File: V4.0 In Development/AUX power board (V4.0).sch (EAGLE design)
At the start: 90 parts, among them U1 ATMEGA328P_TQFP, U2 TPS5405DR, U3 LTC4365HTS8TRMPBFTSOT-23_TS8-M

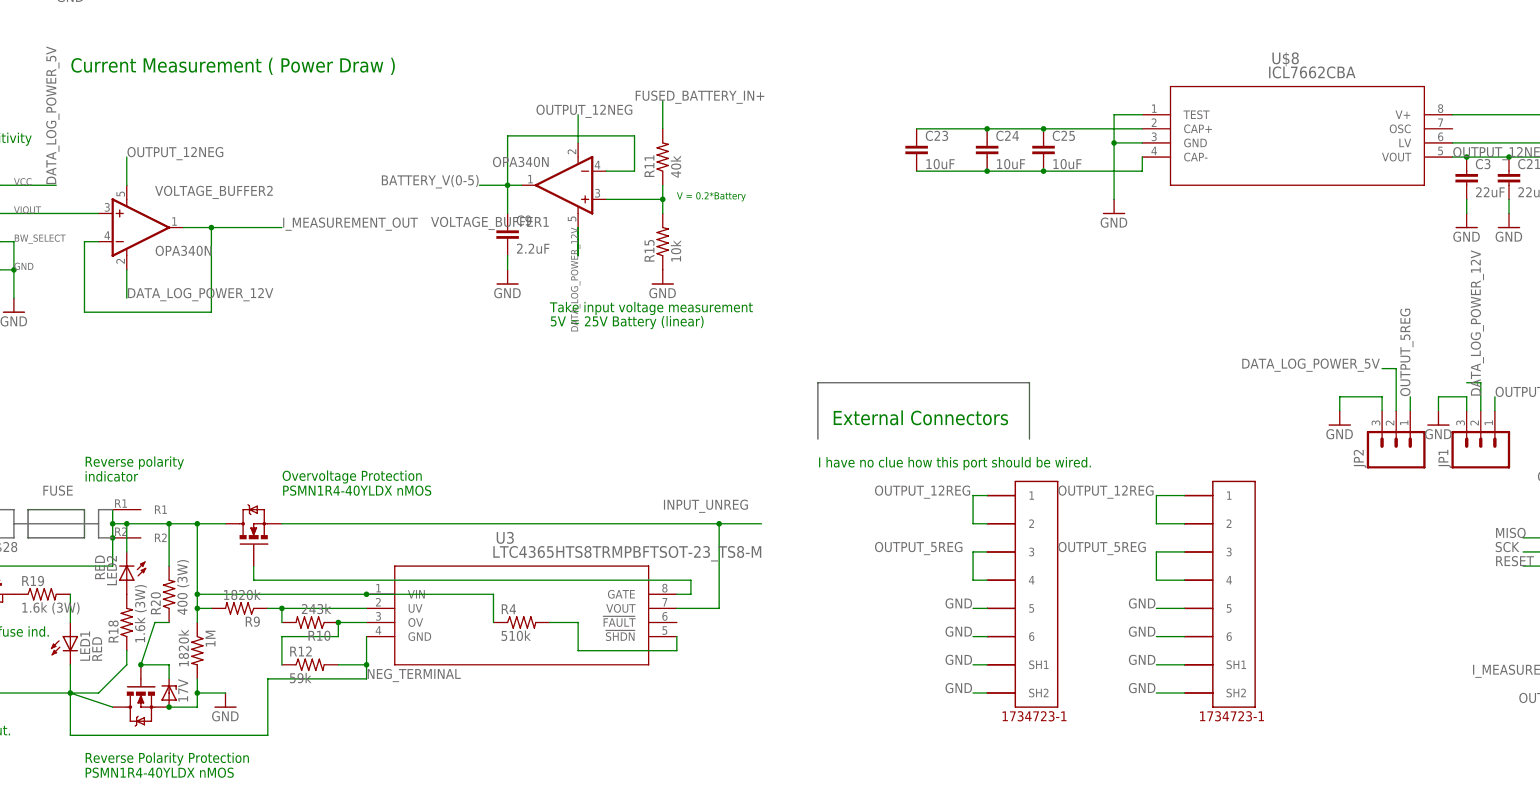
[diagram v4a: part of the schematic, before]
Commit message: Changed to a SOIC opamp
Easier to solder. Had issues with the smaller opamps in the previous
version.

The op-amp i spec'ed out also has a small DC bias (1mV and uses 45uA to
bias)
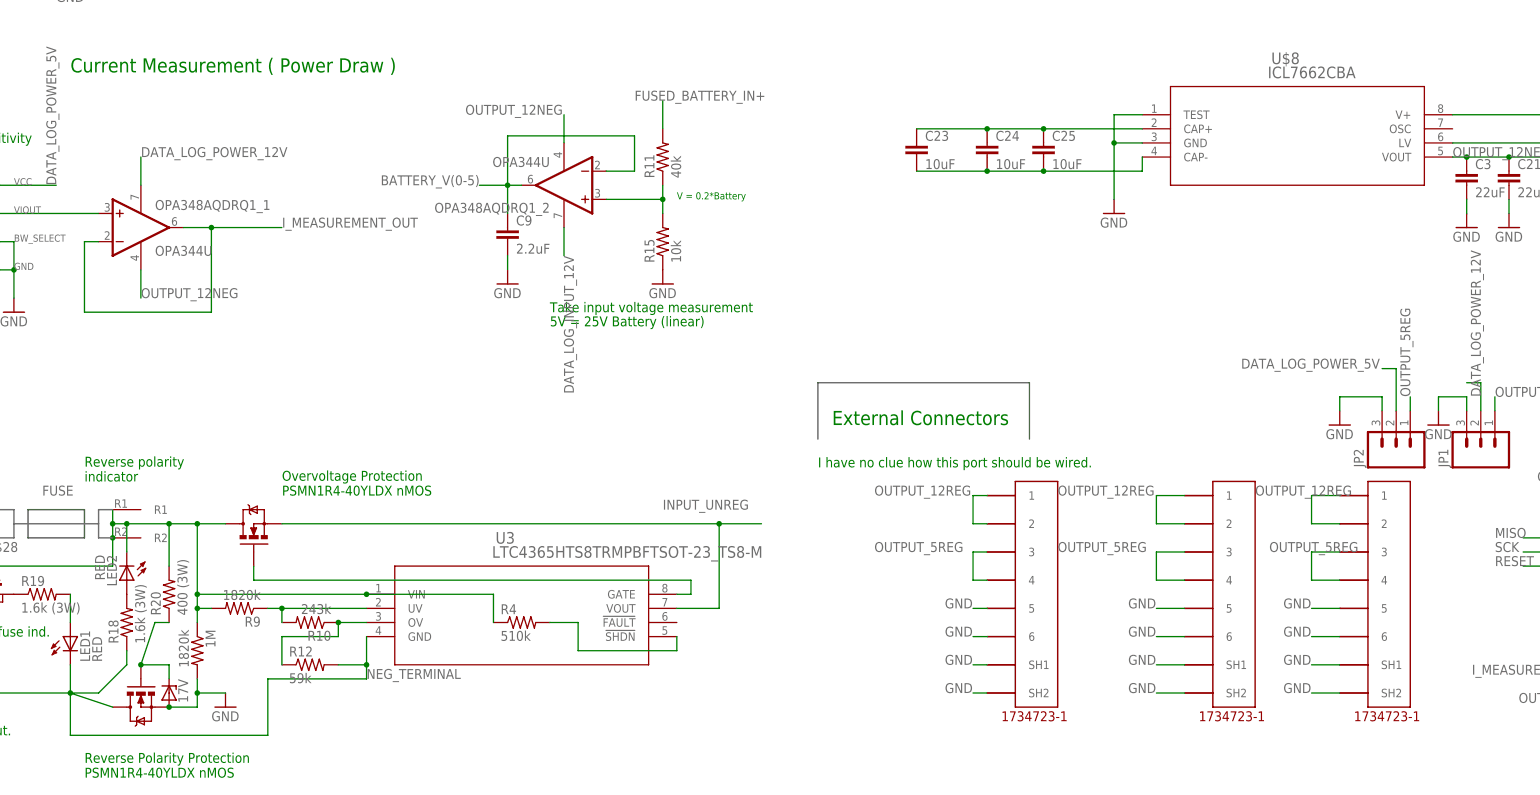
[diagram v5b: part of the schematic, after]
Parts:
- removed VOLTAGE_BUFFER1, VOLTAGE_BUFFER2: OPA340N, burr-brown:OPA340N
- added OPA348AQDRQ1_1, OPA348AQDRQ1_2: OPA344U, linear:OPA344U
- added U$10: 5555140-6, 5555140-6 RJ11:5555140-6
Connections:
- new net DATA_LOG_INPUT_12V: OPA348AQDRQ1_2.V+
- net BATTERY_V(0-5): now also OPA348AQDRQ1_2.-IN, OPA348AQDRQ1_2.OUT; no longer VOLTAGE_BUFFER1.-IN, VOLTAGE_BUFFER1.OUT
- net DATA_LOG_POWER_12V: now also OPA348AQDRQ1_1.V+; no longer VOLTAGE_BUFFER1.V+
- net GND: now also U$10.5, U$10.6, U$10.SH1, U$10.SH2
- net I_MEASUREMENT_OUT: now also OPA348AQDRQ1_1.-IN, OPA348AQDRQ1_1.OUT; no longer VOLTAGE_BUFFER2.-IN, VOLTAGE_BUFFER2.OUT
- net N$12: now also OPA348AQDRQ1_2.+IN; no longer VOLTAGE_BUFFER1.+IN
- net N$2: now also OPA348AQDRQ1_1.+IN; no longer VOLTAGE_BUFFER2.+IN
- net OUTPUT_12NEG: now also OPA348AQDRQ1_1.V-, OPA348AQDRQ1_2.V-; no longer VOLTAGE_BUFFER1.V-, VOLTAGE_BUFFER2.V+
- net OUTPUT_12REG: now also U$10.1, U$10.2
- net OUTPUT_5REG: now also U$10.3, U$10.4
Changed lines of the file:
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@@
 <part name="C6" library="rcl" deviceset="C-EU" device="C0603" value="2.2uF"/>
 <part name="GND17" library="supply1" deviceset="GND" device=""/>
-<part name="VOLTAGE_BUFFER1" library="burr-brown" deviceset="OPA340" device="N"/>
+<part name="OPA348AQDRQ1_2" library="linear" deviceset="OPA*" device="U" technology="344"/>
 <part name="GND20" library="supply1" deviceset="GND" device=""/>
 <part name="GND21" library="supply1" deviceset="GND" device=""/>
@@
 <part name="U1" library="SparkFun-DigitalIC" deviceset="ATMEGA328P_TQFP" device="" value="ATMEGA328P_TQFP"/>
 <part name="U$1" library="linear" deviceset="ACS723" device=""/>
-<part name="VOLTAGE_BUFFER2" library="burr-brown" deviceset="OPA340" device="N"/>
+<part name="OPA348AQDRQ1_1" library="linear" deviceset="OPA*" device="U" technology="344"/>
 <part name="GND7" library="supply1" deviceset="GND" device=""/>
 <part name="U$8" library="linear" deviceset="ICL7662CBA" device=""/>
@@
 <part name="GND35" library="E-P-008-R1.2" deviceset="GND" device=""/>
 <part name="GND36" library="E-P-008-R1.2" deviceset="GND" device=""/>
+<part name="U$10" library="5555140-6 RJ11" deviceset="5555140-6" device=""/>
 </parts>
 <sheets>
@@
 <instance part="C6" gate="G$1" x="347.98" y="187.96"/>
 <instance part="GND17" gate="1" x="347.98" y="177.8"/>
-<instance part="VOLTAGE_BUFFER1" gate="G$1" x="152.4" y="81.28" rot="R180"/>
+<instance part="OPA348AQDRQ1_2" gate="G$1" x="152.4" y="81.28" rot="R180"/>
 <instance part="GND20" gate="1" x="142.24" y="63.5"/>
 <instance part="GND21" gate="1" x="170.18" y="63.5"/>
@@
 <instance part="U1" gate="U$1" x="287.02" y="160.02"/>
 <instance part="U$1" gate="G$1" x="43.18" y="73.66"/>
-<instance part="VOLTAGE_BUFFER2" gate="G$1" x="76.2" y="73.66"/>
+<instance part="OPA348AQDRQ1_1" gate="G$1" x="76.2" y="73.66"/>
 <instance part="GND7" gate="1" x="53.34" y="58.42"/>
 <instance part="U$8" gate="G$1" x="254" y="93.98"/>
@@
 <instance part="GND35" gate="1" x="292.1" y="38.1"/>
 <instance part="GND36" gate="1" x="309.88" y="38.1"/>
+<instance part="U$10" gate="G$1" x="299.72" y="12.7"/>
 </instances>
 <busses>
@@
 <wire x1="320.04" y1="43.18" x2="320.04" y2="40.64" width="0.1524" layer="91"/>
 <label x="320.04" y="43.18" size="1.778" layer="95"/>
+</segment>
+<segment>
+<wire x1="292.1" y1="25.4" x2="287.02" y2="25.4" width="0.1524" layer="91"/>
+<pinref part="U$10" gate="G$1" pin="1"/>
+<wire x1="287.02" y1="25.4" x2="287.02" y2="20.32" width="0.1524" layer="91"/>
+<pinref part="U$10" gate="G$1" pin="2"/>
+<wire x1="287.02" y1="20.32" x2="292.1" y2="20.32" width="0.1524" layer="91"/>
+<label x="276.86" y="25.4" size="1.778" layer="95"/>
 </segment>
 </net>
@@
 <pinref part="GND36" gate="1" pin="GND"/>
 </segment>
+<segment>
+<pinref part="U$10" gate="G$1" pin="5"/>
+<wire x1="292.1" y1="5.08" x2="287.02" y2="5.08" width="0.1524" layer="91"/>
+<label x="281.94" y="5.08" size="1.778" layer="95"/>
+</segment>
+<segment>
+<pinref part="U$10" gate="G$1" pin="6"/>
+<wire x1="292.1" y1="0" x2="287.02" y2="0" width="0.1524" layer="91"/>
+<label x="281.94" y="0" size="1.778" layer="95"/>
+</segment>
+<segment>
+<pinref part="U$10" gate="G$1" pin="SH1"/>
+<wire x1="292.1" y1="-5.08" x2="287.02" y2="-5.08" width="0.1524" layer="91"/>
+<label x="281.94" y="-5.08" size="1.778" layer="95"/>
+</segment>
+<segment>
+<pinref part="U$10" gate="G$1" pin="SH2"/>
+<wire x1="292.1" y1="-10.16" x2="287.02" y2="-10.16" width="0.1524" layer="91"/>
+<label x="281.94" y="-10.16" size="1.778" layer="95"/>
+</segment>
 </net>
 <net name="OUTPUT_5REG" class="0">
@@
 <pinref part="JP2" gate="G$1" pin="1"/>
 <wire x1="304.8" y1="43.18" x2="304.8" y2="40.64" width="0.1524" layer="91"/>
+</segment>
+<segment>
+<pinref part="U$10" gate="G$1" pin="3"/>
+<wire x1="292.1" y1="15.24" x2="287.02" y2="15.24" width="0.1524" layer="91"/>
+<wire x1="287.02" y1="15.24" x2="287.02" y2="10.16" width="0.1524" layer="91"/>
+<pinref part="U$10" gate="G$1" pin="4"/>
+<wire x1="287.02" y1="10.16" x2="292.1" y2="10.16" width="0.1524" layer="91"/>
+<label x="279.4" y="15.24" size="1.778" layer="95"/>
 </segment>
 </net>
@@
 </segment>
 <segment>
-<pinref part="VOLTAGE_BUFFER2" gate="G$1" pin="-IN"/>
+<pinref part="OPA348AQDRQ1_1" gate="G$1" pin="-IN"/>
 <wire x1="68.58" y1="71.12" x2="66.04" y2="71.12" width="0.1524" layer="91"/>
 <wire x1="66.04" y1="71.12" x2="66.04" y2="58.42" width="0.1524" layer="91"/>
 <wire x1="66.04" y1="58.42" x2="88.9" y2="58.42" width="0.1524" layer="91"/>
 <wire x1="88.9" y1="58.42" x2="88.9" y2="73.66" width="0.1524" layer="91"/>
-<pinref part="VOLTAGE_BUFFER2" gate="G$1" pin="OUT"/>
+<pinref part="OPA348AQDRQ1_1" gate="G$1" pin="OUT"/>
 <wire x1="88.9" y1="73.66" x2="83.82" y2="73.66" width="0.1524" layer="91"/>
 <wire x1="88.9" y1="73.66" x2="101.6" y2="73.66" width="0.1524" layer="91"/>
@@
 <segment>
 <wire x1="137.16" y1="81.28" x2="142.24" y2="81.28" width="0.1524" layer="91"/>
-<pinref part="VOLTAGE_BUFFER1" gate="G$1" pin="OUT"/>
+<pinref part="OPA348AQDRQ1_2" gate="G$1" pin="OUT"/>
 <wire x1="142.24" y1="81.28" x2="144.78" y2="81.28" width="0.1524" layer="91"/>
 <wire x1="142.24" y1="81.28" x2="142.24" y2="90.17" width="0.1524" layer="91"/>
@@
 <wire x1="142.24" y1="90.17" x2="165.1" y2="90.17" width="0.1524" layer="91"/>
 <wire x1="165.1" y1="90.17" x2="165.1" y2="83.82" width="0.1524" layer="91"/>
-<pinref part="VOLTAGE_BUFFER1" gate="G$1" pin="-IN"/>
+<pinref part="OPA348AQDRQ1_2" gate="G$1" pin="-IN"/>
 <wire x1="165.1" y1="83.82" x2="160.02" y2="83.82" width="0.1524" layer="91"/>
 <pinref part="C9" gate="G$1" pin="1"/>
@@
 <segment>
 <wire x1="170.18" y1="76.2" x2="170.18" y2="78.74" width="0.1524" layer="91"/>
-<pinref part="VOLTAGE_BUFFER1" gate="G$1" pin="+IN"/>
+<pinref part="OPA348AQDRQ1_2" gate="G$1" pin="+IN"/>
 <wire x1="170.18" y1="78.74" x2="170.18" y2="81.28" width="0.1524" layer="91"/>
 <wire x1="160.02" y1="78.74" x2="170.18" y2="78.74" width="0.1524" layer="91"/>
@@
 <pinref part="U$1" gate="G$1" pin="P$7"/>
 <wire x1="50.8" y1="76.2" x2="68.58" y2="76.2" width="0.1524" layer="91"/>
-<pinref part="VOLTAGE_BUFFER2" gate="G$1" pin="+IN"/>
+<pinref part="OPA348AQDRQ1_1" gate="G$1" pin="+IN"/>
 </segment>
 </net>
@@
 </segment>
 <segment>
-<pinref part="VOLTAGE_BUFFER2" gate="G$1" pin="V+"/>
-<wire x1="73.66" y1="81.28" x2="73.66" y2="86.36" width="0.1524" layer="91"/>
-<label x="73.66" y="86.36" size="1.778" layer="95"/>
-</segment>
-<segment>
-<pinref part="VOLTAGE_BUFFER1" gate="G$1" pin="V-"/>
-<wire x1="154.94" y1="88.9" x2="154.94" y2="93.98" width="0.1524" layer="91"/>
-<label x="147.32" y="93.98" size="1.778" layer="95"/>
+<pinref part="OPA348AQDRQ1_1" gate="G$1" pin="V-"/>
+<wire x1="76.2" y1="66.04" x2="76.2" y2="60.96" width="0.1524" layer="91"/>
+<label x="76.2" y="60.96" size="1.778" layer="95"/>
+</segment>
+<segment>
+<pinref part="OPA348AQDRQ1_2" gate="G$1" pin="V-"/>
+<wire x1="152.4" y1="88.9" x2="152.4" y2="93.98" width="0.1524" layer="91"/>
+<label x="134.62" y="93.98" size="1.778" layer="95"/>
 </segment>
 </net>
@@
 </segment>
 <segment>
-<pinref part="VOLTAGE_BUFFER1" gate="G$1" pin="V+"/>
-<wire x1="154.94" y1="73.66" x2="154.94" y2="68.58" width="0.1524" layer="91"/>
-<label x="154.94" y="73.66" size="1.27" layer="95" rot="MR270"/>
-<wire x1="154.94" y1="73.66" x2="154.94" y2="68.58" width="0.1524" layer="91"/>
-</segment>
-<segment>
-<wire x1="73.66" y1="66.04" x2="73.66" y2="60.96" width="0.1524" layer="91"/>
-<label x="73.66" y="60.96" size="1.778" layer="95"/>
-</segment>
-</net>
+<pinref part="OPA348AQDRQ1_1" gate="G$1" pin="V+"/>
+<wire x1="76.2" y1="81.28" x2="76.2" y2="86.36" width="0.1524" layer="91"/>
+<label x="76.2" y="86.36" size="1.778" layer="95"/>
+</segment>
+</net>
+<net name="DATA_LOG_INPUT_12V" class="0">
+<segment>
+<pinref part="OPA348AQDRQ1_2" gate="G$1" pin="V+"/>
+<wire x1="152.4" y1="73.66" x2="152.4" y2="68.58" width="0.1524" layer="91"/>
+<label x="152.4" y="68.58" size="1.778" layer="95" rot="R270"/>
+</segment>
+</net>

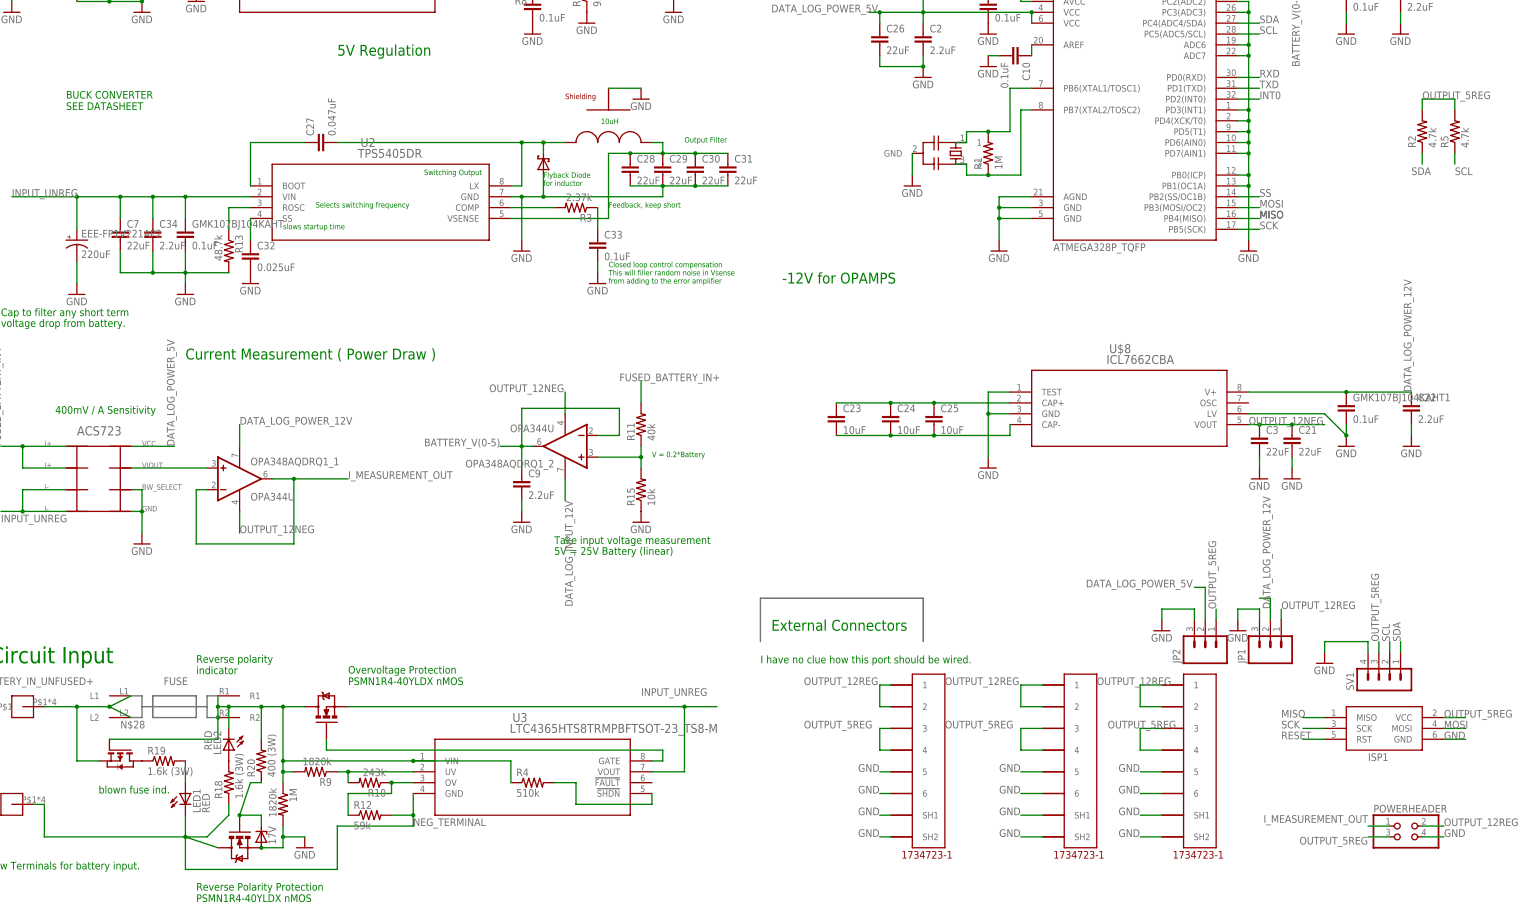
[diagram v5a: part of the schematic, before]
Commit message: Made some changes to protection
Desided to make a crowbar for overvoltage instead.
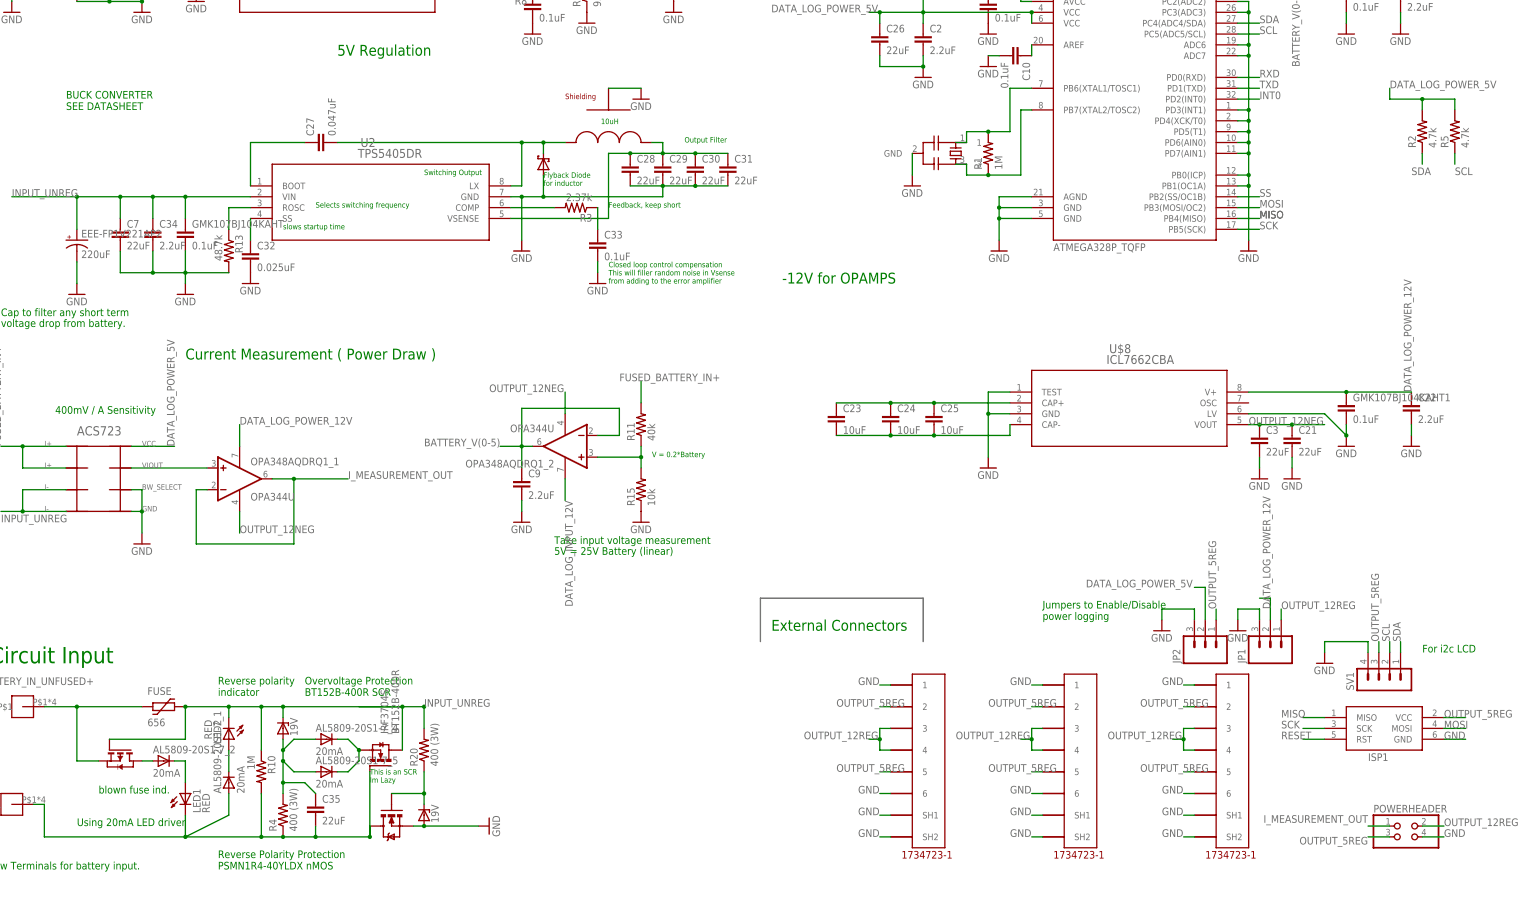
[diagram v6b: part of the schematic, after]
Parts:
- removed 1M, R9: 1820k, rcl:R-US_R0805
- removed MINIBLADE: 3568, fuse:3568
- removed PSMN1R4-40TLDX: MOSFET-NCHANNELFDS6630A, PSMN1R4-40YLDX:MOSFET-NCHANNELFDS6630A
- removed R12: 59k, rcl:R-US_R0805
- removed R18, R19: 1.6k (3W), resistor:R-US_R2512
- removed TN2540-600G-TR: 17V, diode:ZENER-DIODEDO41Z10
- removed U3: LTC4365HTS8TRMPBFTSOT-23_TS8-M, LTC4365:LTC4365HTS8TRMPBFTSOT-23_TS8-M
- added 1N5356BRLG_1, 1N5356BRLG_2: 19V, diode:ZENER-DIODEDO41Z10
- added AL5809-20S1-7_1, AL5809-20S1-7_2, AL5809-20S1-7_4, AL5809-20S1-7_5: 20mA, semicon-smd-ipc:D-SOD123
- added BT152B-400R: IRF3704S, transistor-power:IRF3704S
- added C35: 22uF, rcl:C-EUC1210
- added FUSE: 656, GlassFuseHolder:656
- R10: value 243k -> 1M
- R4: value 510k -> 400 (3W); device rcl:R-US_R0805 -> resistor:R-US_R2512
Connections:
- removed net N$28: 1M.1, LED2.C, MINIBLADE.R1, MINIBLADE.R2, PSMN1R4-40TLDX.D, R20.2, R4.1, R9.2, U3.VIN, ZVP4525E6TA_1.G
- removed net N$31: R4.2, U3.!SHDN
- removed net N$32: LED2.A, R18.2
- removed net N$33: PSMN1R4-40TLDX.G, U3.GATE
- new net N$22: AL5809-20S1-7_1.C, LED2.A
- net BATTERY_IN_UNFUSED+: now also FUSE.1; no longer MINIBLADE.L1, MINIBLADE.L2
- net DATA_LOG_POWER_5V: now also R2.2, R5.2
- net GND: now also 1N5356BRLG_1.A; no longer 1M.2, TN2540-600G-TR.A, U$10.5, U$3.5, U$4.5
- net INPUT_UNREG: now also 1N5356BRLG_2.C, BT152B-400R.D, FUSE.2, LED2.C, R10.1, R20.2, ZVP4525E6TA_1.G; no longer PSMN1R4-40TLDX.S, U3.VOUT
- net N$17: now also AL5809-20S1-7_2.A; no longer R19.1
- net N$19: now also 1N5356BRLG_1.C; no longer TN2540-600G-TR.C
- net N$25: now also AL5809-20S1-7_2.C; no longer R19.2
- net N$29: now also 1N5356BRLG_2.A, AL5809-20S1-7_4.A, AL5809-20S1-7_5.A, C35.1, R4.2; no longer R10.2, R9.1, U3.UV
- net N$30: now also AL5809-20S1-7_4.C, AL5809-20S1-7_5.C, BT152B-400R.S; no longer R10.1, R12.1, U3.OV
- net NEG_TERMINAL: now also AL5809-20S1-7_1.A, BT152B-400R.G, C35.2, R10.2, R4.1; no longer R12.2, R18.1, U3.GND
- net OUTPUT_12REG: now also U$10.3, U$10.4, U$3.3, U$3.4, U$4.3, U$4.4; no longer U$10.1, U$10.2, U$3.1, U$3.2, U$4.1, U$4.2
- net OUTPUT_5REG: now also U$10.2, U$10.5, U$3.2, U$3.5, U$4.2, U$4.5; no longer R2.2, R5.2, U$10.3, U$10.4, U$3.3, U$3.4, U$4.3, U$4.4
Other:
- note added: "For i2c LCD"
- note added: "Jumpers to Enable/Disable power logging"
- note added: "Overvoltage Protection BT152B-400R SCR"
- note added: "This is an SCR Im Lazy"
- note added: "Using 20mA LED driver"
- note removed: "I have no clue how this port should be wired."
- note removed: "Overvoltage Protection PSMN1R4-40YLDX nMOS"
- moved on the sheet: LED2, R10, R20, R4
